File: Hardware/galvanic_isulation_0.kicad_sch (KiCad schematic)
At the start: 14 parts

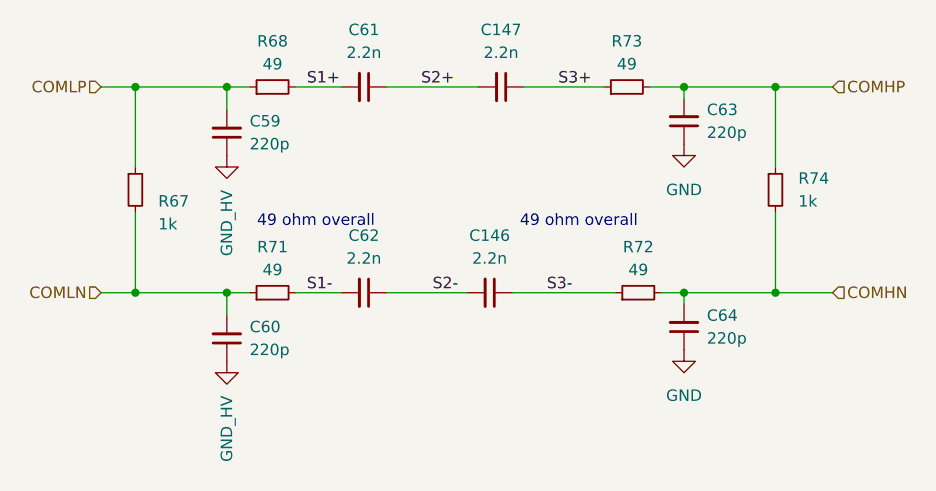
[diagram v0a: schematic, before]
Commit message: Zmiany wizualne w schemacie
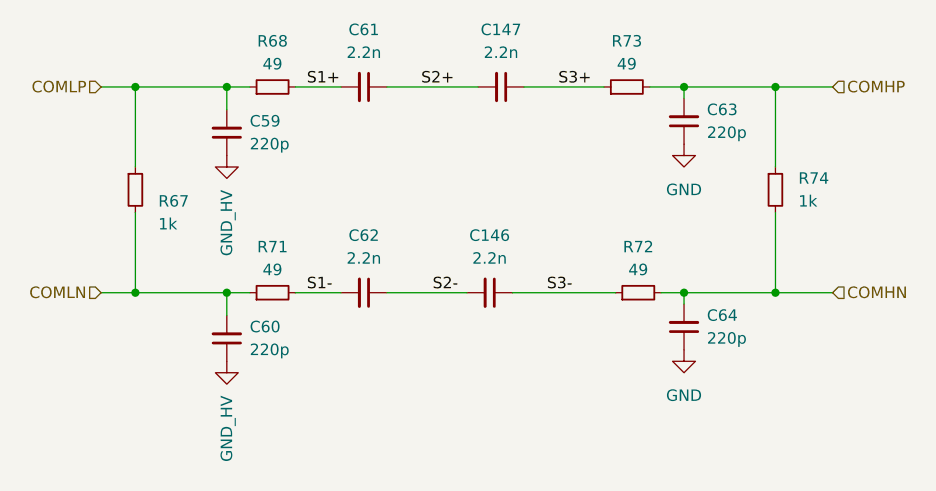
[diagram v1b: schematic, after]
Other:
- note removed: "49 ohm overall"
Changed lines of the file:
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@@
 	(generator_version "9.0")
 	(paper "A4")
-	(text "49 ohm overall\n"
-		(exclude_from_sim no)
-		(at 103.886 89.916 0)
-		(effects
-			(font
-				(size 1.27 1.27)
-			)
-		)
-	)
-	(text "49 ohm overall\n"
-		(exclude_from_sim no)
-		(at 133.096 89.916 0)
-		(effects
-			(font
-				(size 1.27 1.27)
-			)
-		)
-	)
 	(junction
 		(at 83.82 74.93)
